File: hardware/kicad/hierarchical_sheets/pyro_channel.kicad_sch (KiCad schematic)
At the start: 35 parts, among them J2 282834-4, U2 ZXCT1110W5-7, U3 SI9926CDY

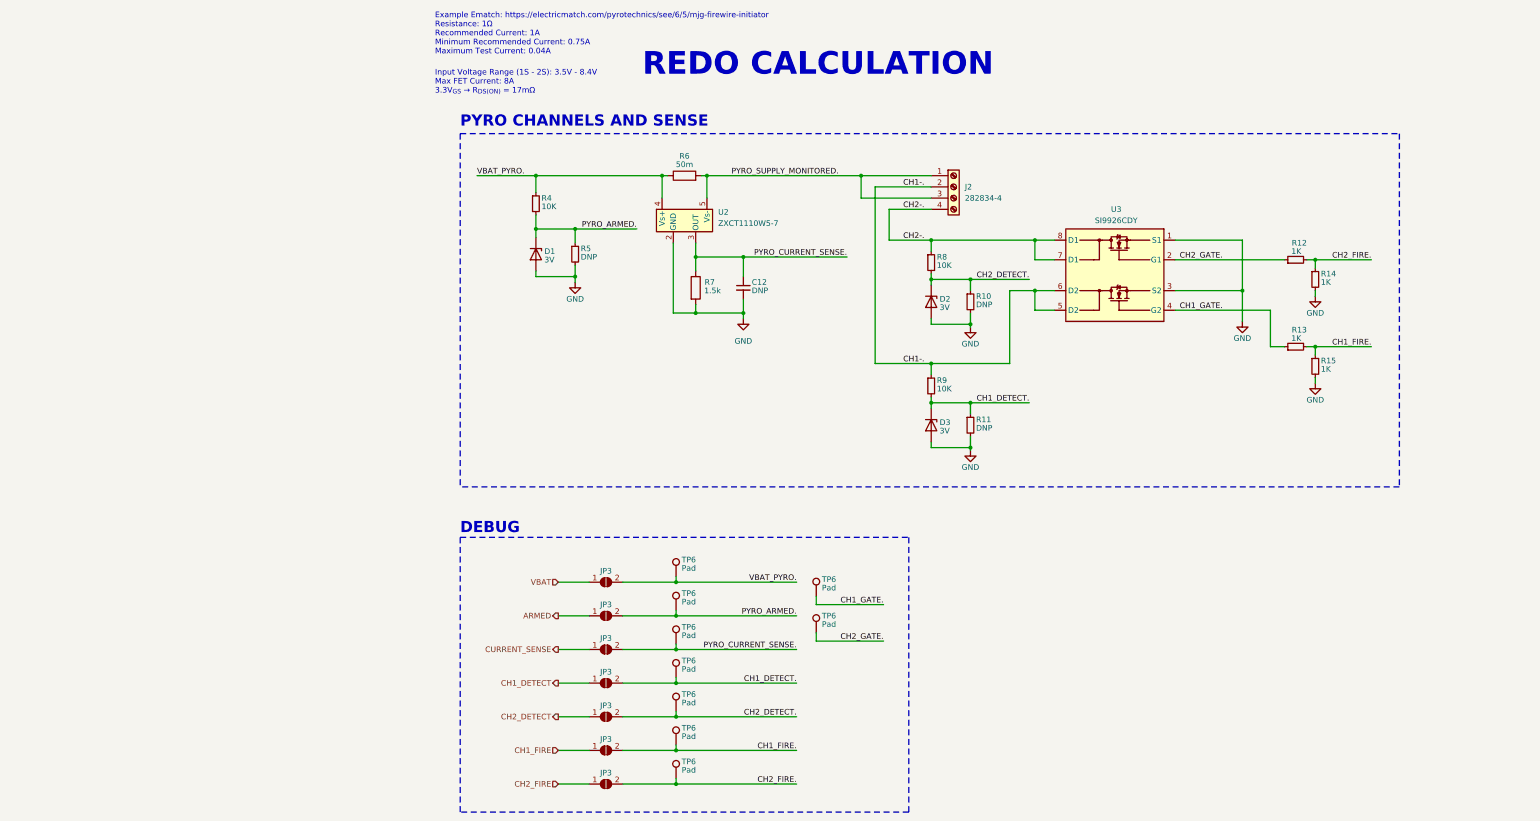
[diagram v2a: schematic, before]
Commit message: Updated labels
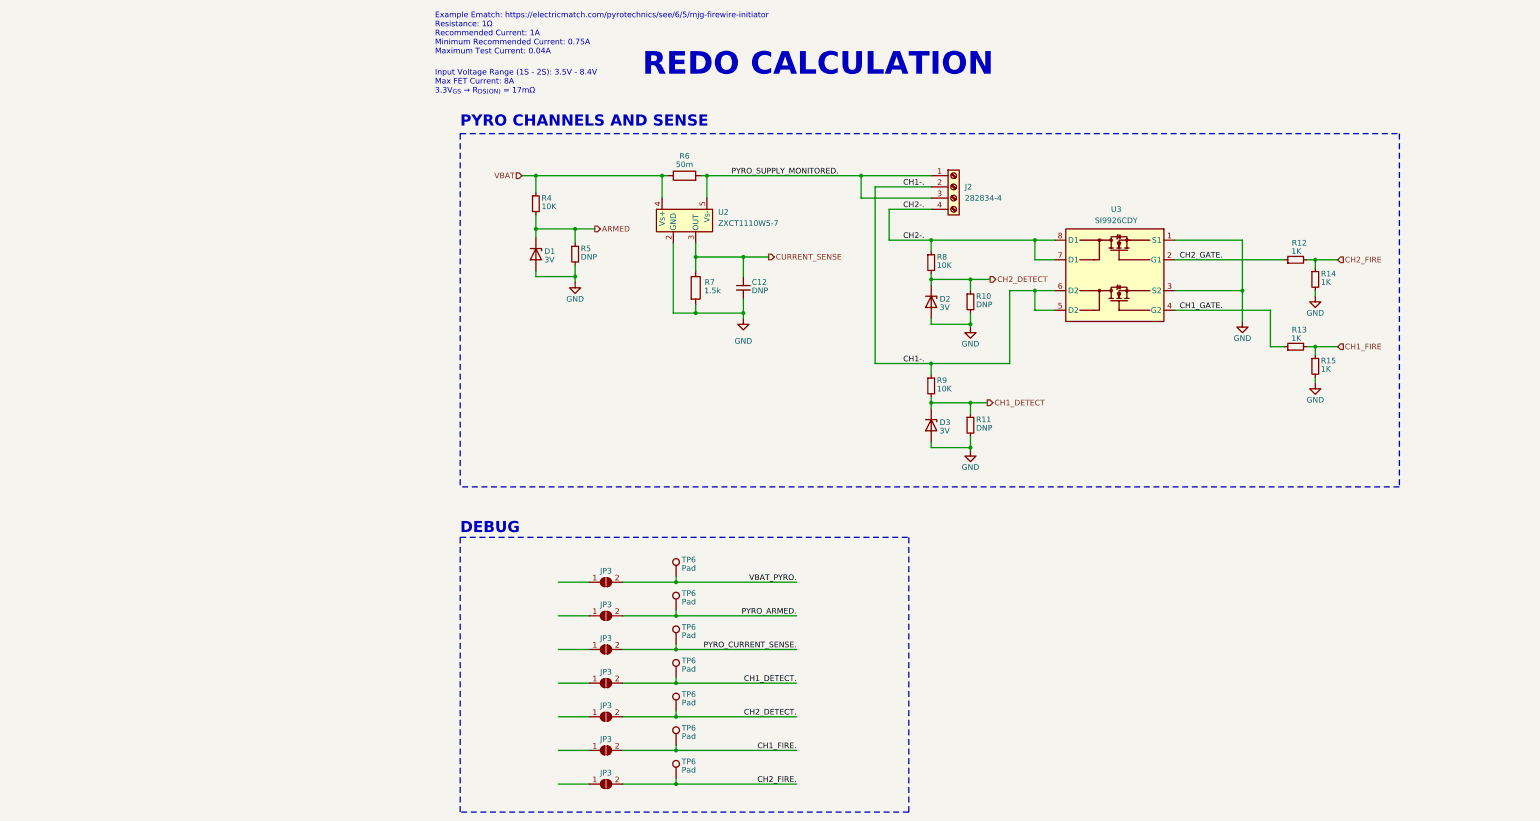
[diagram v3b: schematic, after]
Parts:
- removed TP6 (x2): Pad, TestPoint:TestPoint_Pad_D1.0mm, symbol Connector:TestPoint
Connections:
- net ARMED: now also D1.3 (K), R4.2, R5.1; no longer JP3.1 (A)
- net CH1_DETECT: now also D3.3 (K), R11.1, R9.2; no longer JP3.1 (A)
- net CH1_DETECT.: no longer D3.3 (K), R11.1, R9.2
- net CH1_FIRE: now also R13.2, R15.1; no longer JP3.1 (A)
- net CH1_FIRE.: no longer R13.2, R15.1
- net CH2_DETECT: now also D2.3 (K), R10.1, R8.2; no longer JP3.1 (A)
- net CH2_DETECT.: no longer D2.3 (K), R10.1, R8.2
- net CH2_FIRE: now also R12.2, R14.1; no longer JP3.1 (A)
- net CH2_FIRE.: no longer R12.2, R14.1
- net CURRENT_SENSE: now also C12.1, R7.1, U2.3 (OUT); no longer JP3.1 (A)
- net PYRO_ARMED.: no longer D1.3 (K), R4.2, R5.1
- net PYRO_CURRENT_SENSE.: no longer C12.1, R7.1, U2.3 (OUT)
- net VBAT: now also R4.1, R6.1, U2.4 (Vs+); no longer JP3.1 (A)
- net VBAT_PYRO.: no longer R4.1, R6.1, U2.4 (Vs+)

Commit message: fixed
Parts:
- removed JP3 (x7): SolderJumper_2_Open, Jumper:SolderJumper-2_P1.3mm_Open_RoundedPad1.0x1.5mm, symbol Jumper:SolderJumper_2_Open
- removed TP6 (x7): Pad, TestPoint:TestPoint_Pad_D1.0mm, symbol Connector:TestPoint
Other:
- note removed: "DEBUG"

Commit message: file sync
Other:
- note added: "Example Ematch: https://electricmatch.com/pyrotechnics/see/6/5/mjg-firewire-initiator--standard Resistance: 1Ω Recommended Current: 1A Minimum Recommended Current: 0.75A Maximum Test Current: 0.04A"
- note removed: "Example Ematch: https://electricmatch.com/pyrotechnics/see/6/5/mjg-firewire-initiator Resistance: 1Ω Recommended Current: 1A Minimum Recommended Current: 0.75A Maximum Test Current: 0.04A"
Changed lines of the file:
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@@
     (effects (font (size 1.27 1.27)) (justify left bottom))
   )
-  (text "Example Ematch: https://electricmatch.com/pyrotechnics/see/6/5/mjg-firewire-initiator\nResistance: 1Ω\nRecommended Current: 1A\nMinimum Recommended Current: 0.75A\nMaximum Test Current: 0.04A\n"
+  (text "Example Ematch: https://electricmatch.com/pyrotechnics/see/6/5/mjg-firewire-initiator--standard\nResistance: 1Ω\nRecommended Current: 1A\nMinimum Recommended Current: 0.75A\nMaximum Test Current: 0.04A\n"
     (at 13.335 22.86 0)
     (effects (font (size 1.27 1.27)) (justify left bottom))

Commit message: added power and checked schematics
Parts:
- added J7: Screw_Terminal_01x02, symbol Connector:Screw_Terminal_01x02
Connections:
- net VBAT: now also J7.1 (Pin_1); no longer R4.1, R6.1, U2.4 (Vs+)
- new net: J7.2 (Pin_2), R4.1, R6.1, U2.4 (Vs+)
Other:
- moved on the sheet: C12, D1, D2, D3, J2, R10, R11, R12, R13, R14, R15, R4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

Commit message: assigned footprints
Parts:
- C3: renamed from C12; footprint Capacitor_SMD:C_0402_1005Metric -> Resistor_SMD:R_0603_1608Metric
- renumbered D1 to D3, D2 to D4, D3 to D5, J7 to J2, J2 to J3, R4 to R1, R13 to R10, R14 to R11, R15 to R12, R5 to R2, R6 to R3, R7 to R4, R8 to R5, R9 to R6, R10 to R7, R11 to R8, R12 to R9

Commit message: making formatting more consistent
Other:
- note added: "Chosen MOSFET: https://www.digikey.com/en/products/detail/vishay-siliconix/SI9926CDY-T1-GE3/1978863 Max Continous FET Current: 8A Max Pulse FET Current: 30A 3.3V_{GS} → R_{DS(ON)} = 17mΩ"
- note added: "EMATCH:"
- note added: "FET:"
- note removed: "Input Voltage Range (1S - 2S): 3.5V - 8.4V Max FET Current: 8A 3.3V_{GS} → R_{DS(ON)} = 17mΩ"
- moved on the sheet: C3, D3, D4, D5, J2, J3, R1, R10, R11, R12, R2, R3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
